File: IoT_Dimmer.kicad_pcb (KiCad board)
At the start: 2 copper layers, 1 part

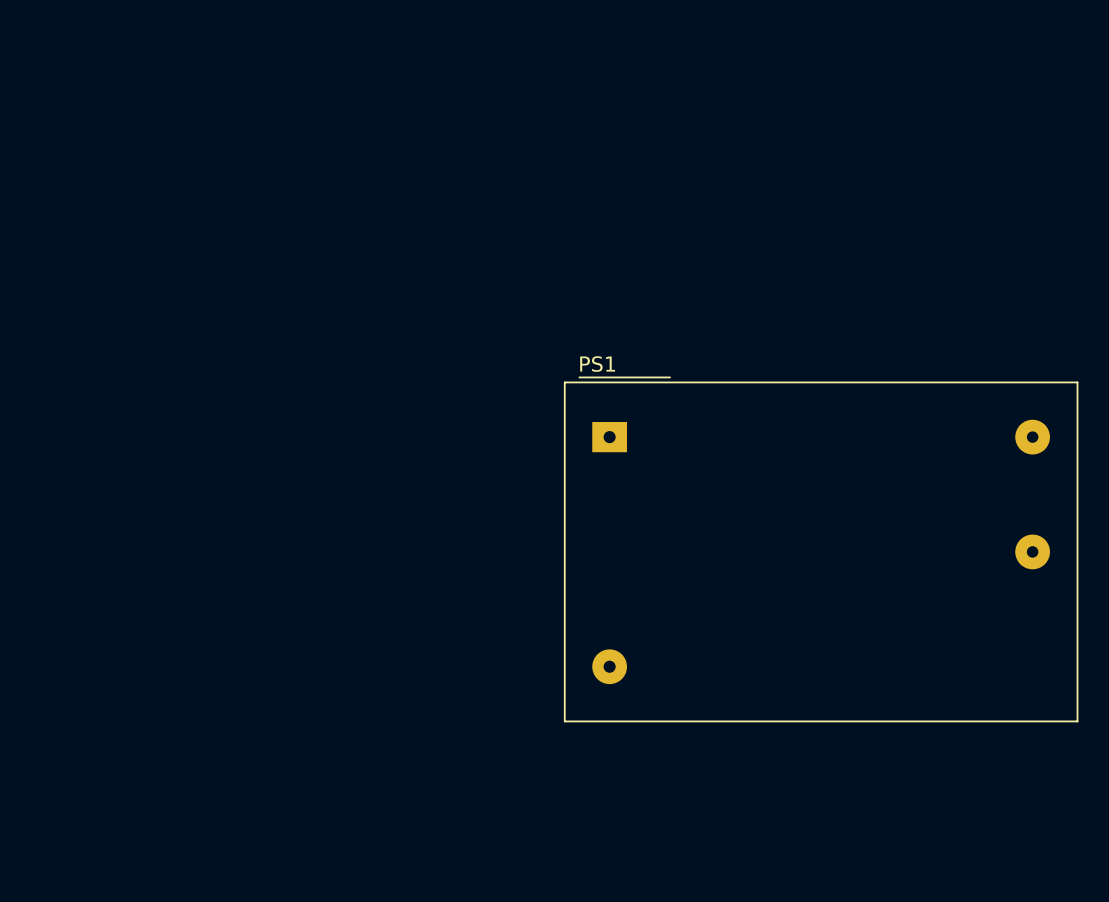
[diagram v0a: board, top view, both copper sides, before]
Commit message: Power esp32
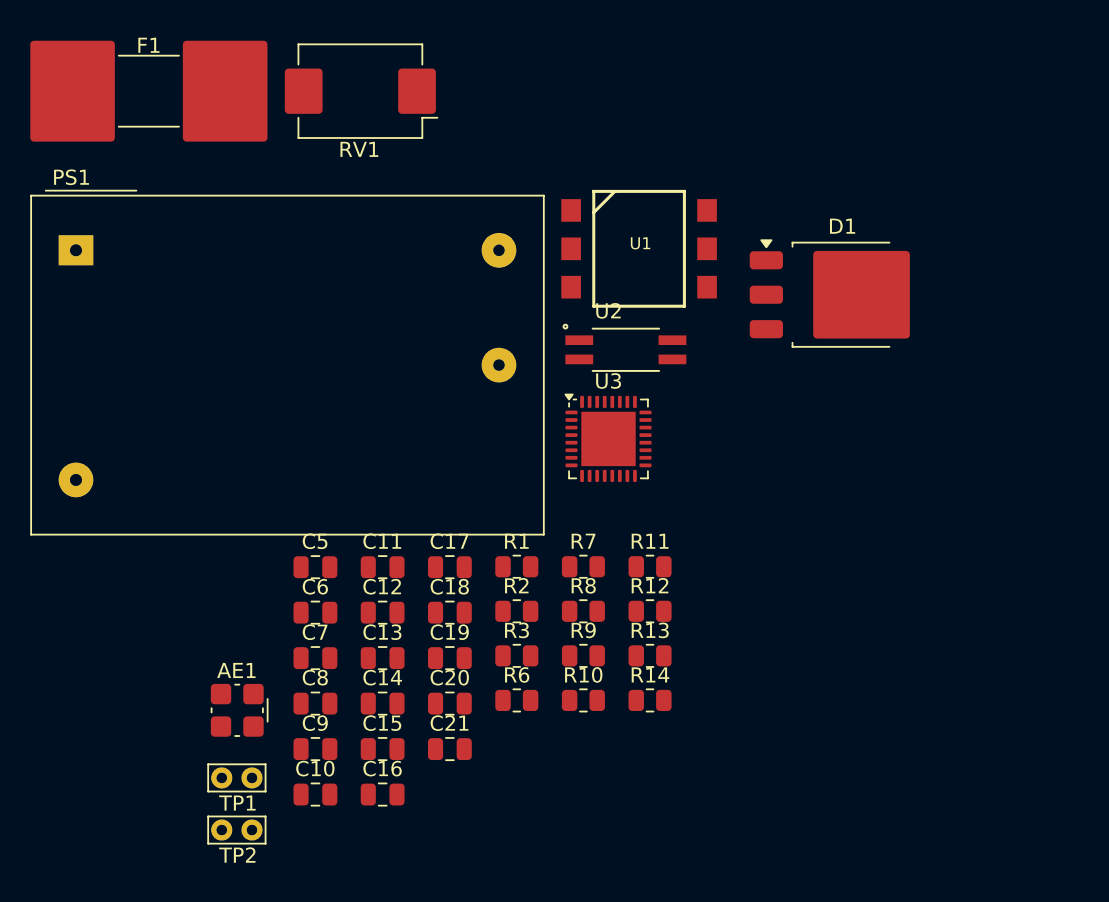
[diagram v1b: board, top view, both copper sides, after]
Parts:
- added AE1: Antenna, RF_Antenna:Molex_47948-0001_2.4Ghz, F.Cu at (119.8, 90.5)
- added C10: 0.1uF, Capacitor_SMD:C_0805_2012Metric, F.Cu at (125.0, 96.1)
- added C11: 0.1uF, Capacitor_SMD:C_0805_2012Metric, F.Cu at (129.5, 81.0)
- added C12: 0.1uF, Capacitor_SMD:C_0805_2012Metric, F.Cu at (129.5, 84.0)
- added C13: 1uF, Capacitor_SMD:C_0805_2012Metric, F.Cu at (129.5, 87.0)
- added C14: 0.1uF, Capacitor_SMD:C_0805_2012Metric, F.Cu at (129.5, 90.0)
- added C15: 0.1uF, Capacitor_SMD:C_0805_2012Metric, F.Cu at (129.5, 93.0)
- added C16: 10nF, Capacitor_SMD:C_0805_2012Metric, F.Cu at (129.5, 96.1)
- added C17: 1uF, Capacitor_SMD:C_0805_2012Metric, F.Cu at (133.9, 81.0)
- added C18: 0.1uF, Capacitor_SMD:C_0805_2012Metric, F.Cu at (133.9, 84.0)
- added C19: 0.1uF, Capacitor_SMD:C_0805_2012Metric, F.Cu at (133.9, 87.0)
- added C20: 0.1uF, Capacitor_SMD:C_0805_2012Metric, F.Cu at (133.9, 90.0)
- added C21: 0.1uF, Capacitor_SMD:C_0805_2012Metric, F.Cu at (133.9, 93.0)
- added C5: 10pF, Capacitor_SMD:C_0805_2012Metric, F.Cu at (125.0, 81.0)
- added C6: 10pF, Capacitor_SMD:C_0805_2012Metric, F.Cu at (125.0, 84.0)
- added C7: 0.1uF, Capacitor_SMD:C_0805_2012Metric, F.Cu at (125.0, 87.0)
- added C8: 0.1uF, Capacitor_SMD:C_0805_2012Metric, F.Cu at (125.0, 90.0)
- added C9: 4.7uF, Capacitor_SMD:C_0805_2012Metric, F.Cu at (125.0, 93.0)
- added D1: BTA204S-800, Package_TO_SOT_SMD:TO-252-3_TabPin2, F.Cu at (159.9, 63.0)
- added F1: 2A, Fuse:Fuse_Littelfuse-NANO2-462, F.Cu at (114.0, 49.5)
- added R1: 360, Resistor_SMD:R_0805_2012Metric, F.Cu at (138.4, 81.0)
- added R10: 510, Resistor_SMD:R_0805_2012Metric, F.Cu at (142.8, 89.8)
- added R11: 10k, Resistor_SMD:R_0805_2012Metric, F.Cu at (147.2, 81.0)
- added R12: 10k, Resistor_SMD:R_0805_2012Metric, F.Cu at (147.2, 83.9)
- added R13: 10k, Resistor_SMD:R_0805_2012Metric, F.Cu at (147.2, 86.9)
- added R14: 10k, Resistor_SMD:R_0805_2012Metric, F.Cu at (147.2, 89.8)
- added R2: 470, Resistor_SMD:R_0805_2012Metric, F.Cu at (138.4, 83.9)
- added R3: 39, Resistor_SMD:R_0805_2012Metric, F.Cu at (138.4, 86.9)
- added R6: 10k, Resistor_SMD:R_0805_2012Metric, F.Cu at (138.4, 89.8)
- added R7: 10k, Resistor_SMD:R_0805_2012Metric, F.Cu at (142.8, 81.0)
- added R8: 10k, Resistor_SMD:R_0805_2012Metric, F.Cu at (142.8, 83.9)
- added R9: 500, Resistor_SMD:R_0805_2012Metric, F.Cu at (142.8, 86.9)
- added RV1: Varistor, Varistor:Varistor_Panasonic_VF, F.Cu at (128.0, 49.5)
- added TP1: RST, TestPoint:TestPoint_Bridge_Pitch2.0mm_Drill0.7mm, F.Cu at (118.8, 95.0)
- added TP2: BOOT, TestPoint:TestPoint_Bridge_Pitch2.0mm_Drill0.7mm, F.Cu at (118.8, 98.4)
- added U1: MOC3021S, MOC3021SM:DIP6_SMD, F.Cu at (146.4, 59.9)
- added U2: VOS628AT, VOS628AT:SOIC127P700X210-4N, F.Cu at (145.6, 66.6)
- added U3: ESP32-C6FH4, Package_DFN_QFN:QFN-32-1EP_5x5mm_P0.5mm_EP3.6x3.6mm, F.Cu at (144.4, 72.5)
- moved PS1 37.4 mm to (109.2, 60.0)
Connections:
- PS1 pad 1: unconnected-(PS1-AC/N-Pad1) -> Net-(D1-A2)
- PS1 pad 2: unconnected-(PS1-AC/L-Pad2) -> Net-(J1-Pin_1)
- PS1 pad 3: unconnected-(PS1--Vo-Pad3) -> GND
- PS1 pad 4: unconnected-(PS1-+Vo-Pad4) -> +3V3

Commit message: PCB_start
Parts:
- added C1: 0.05uF, Capacitor_SMD:C_1812_4532Metric, F.Cu at (174.2, 34.2)
- added C2: 22nF, Capacitor_SMD:C_1812_4532Metric, F.Cu at (194.7, 52.1)
- added C3: C, Capacitor_SMD:C_0603_1608Metric, F.Cu at (162.6, 85.4)
- added C4: C, Capacitor_SMD:C_0603_1608Metric, F.Cu at (162.6, 88.4)
- added J2: Screw_Terminal_01x02, Wago_2059-302998-403:CONN2_2059-302&slash_998-403_WAG, F.Cu at (181.5, 12.5)
- added L1: L, Inductor_SMD:L_0805_2012Metric, F.Cu at (167.1, 85.3)
- added L2: 0.1nH, Inductor_SMD:L_0805_2012Metric, F.Cu at (167.1, 88.0)
- added R4: 75k, Resistor_SMD:R_1206_3216Metric, F.Cu at (168.5, 51.8)
- added R5: 75k, Resistor_SMD:R_1206_3216Metric, F.Cu at (168.5, 48.0)
- added Y2: Crystal_GND24, Crystal:Crystal_SMD_2016-4Pin_2.0x1.6mm, F.Cu at (161.2, 97.0)
- C10, C11, C12, C13, C14, C15, C16, C17, C18, C19, C20, C21, C5, C6, C7, C8, C9: footprint Capacitor_SMD:C_0805_2012Metric -> Capacitor_SMD:C_0603_1608Metric
- F1: value 2A -> 3A
- R1, R2, R3: footprint Resistor_SMD:R_0805_2012Metric -> Resistor_SMD:R_1206_3216Metric
- R10, R11, R12, R13, R14, R6, R7, R8, R9: footprint Resistor_SMD:R_0805_2012Metric -> Resistor_SMD:R_0603_1608Metric
- RV1: footprint Varistor:Varistor_Panasonic_VF -> Varistor:RV_Disc_D7mm_W3.4mm_P5mm
- moved RV1 62.1 mm to (184.0, 22.6)
- moved R2 58.0 mm to (175.0, 39.0)
- moved R1 50.6 mm to (171.8, 43.0)
- moved C5 41.8 mm to (163.7, 97.0), turned to -90 degrees
- moved U3 39.1 mm to (162.8, 107.0)
- moved C17 36.4 mm to (163.4, 102.4)
- moved R3 36.4 mm to (171.5, 72.0)
- moved C6 36.1 mm to (158.8, 97.0), turned to 90 degrees
- moved D1 34.8 mm to (185.2, 39.0)
- moved R9 33.7 mm to (170.0, 106.8)
- moved C16 30.8 mm to (159.5, 103.1), turned to 180 degrees
- moved F1 30.0 mm to (108.5, 20.0)
- moved U1 28.1 mm to (162.2, 36.7)
- moved U2 22.9 mm to (160.8, 49.5), turned to 180 degrees
- moved C15 20.8 mm to (147.5, 103.5)
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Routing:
- net /xtal_p: track 0.00 -> 1.86 mm
- net /xtal_n: track 0.00 -> 1.82 mm

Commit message: CPU_STAND
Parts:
- C2: renamed from C4; footprint Capacitor_SMD:C_0603_1608Metric -> Capacitor_SMD:C_0402_1005Metric
- C4: renamed from C3; footprint Capacitor_SMD:C_0603_1608Metric -> Capacitor_SMD:C_0402_1005Metric
- L1: footprint Inductor_SMD:L_0805_2012Metric -> Inductor_SMD:L_0402_1005Metric
- L2: footprint Inductor_SMD:L_0805_2012Metric -> Inductor_SMD:L_0603_1608Metric
- moved C8 81.6 mm to (167.4, 156.2), turned to 180 degrees
- moved R2 81.1 mm to (173.7, 155.9), turned to -90 degrees
- moved C6 80.8 mm to (171.9, 155.9), turned to -90 degrees
- moved C10 80.4 mm to (166.3, 152.5), turned to -90 degrees
- moved C7 77.6 mm to (167.4, 154.8), turned to 180 degrees
- moved R3 77.0 mm to (170.1, 155.9), turned to -90 degrees
- moved C1 76.4 mm to (164.5, 152.5), turned to -90 degrees
- moved C11 72.0 mm to (175.7, 145.2), turned to 90 degrees
- moved AE1 69.7 mm to (165.1, 143.4), turned to 180 degrees
- moved R1 67.3 mm to (162.8, 152.5), turned to -90 degrees
- moved L2 64.5 mm to (168.1, 152.5), turned to 90 degrees
- moved C4 63.8 mm to (165.7, 149.1), turned to 180 degrees
- moved L1 62.4 mm to (166.2, 147.6), turned to -90 degrees
- moved C2 57.8 mm to (165.7, 146.2), turned to 180 degrees
- moved C9 57.8 mm to (167.4, 157.8), turned to 180 degrees
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- renumbered C7 to C1, C11 to C10, C14 to C11, C16 to C12, C17 to C13, C10 to C14, C9 to C15, C21 to C16, C19 to C17, C1 to C19, C2 to C21, C5 to C3, C6 to C5, C8 to C6, C13 to C7, C12 to C8, C15 to C9, R6 to R1, R4 to R10, R5 to R11, R1 to R12, R2 to R13, R3 to R14, R7 to R2, R8 to R3, R9 to R4, R11 to R5, R10 to R6, R12 to R7, R13 to R8, R14 to R9, TP2 to TP1, TP1 to TP2, U3 to U1, U1 to U3, Y2 to Y1
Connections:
- net /xtal_n renamed /XTAL_N
- net /xtal_p renamed /XTAL_P
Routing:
- net Net-(U1-ANT): track 0.00 -> 3.44 mm
- net Net-(AE1-A): track 0.00 -> 2.64 mm
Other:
- copper layers 2 -> 4

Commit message: pcb
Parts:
- removed TP1: BOOT, TestPoint:TestPoint_Bridge_Pitch2.0mm_Drill0.7mm
- removed TP2: RST, TestPoint:TestPoint_Bridge_Pitch2.0mm_Drill0.7mm
- PS1: moved to B.Cu
- moved C3 74.9 mm to (99.8, 153.9), turned to 0 degrees
- moved PS1 74.4 mm to (128.0, 144.1), turned to 180 degrees
- moved C11 74.2 mm to (101.7, 150.9)
- moved Y1 73.1 mm to (99.7, 156.2), turned to 90 degrees
- moved R4 72.3 mm to (106.9, 149.1), turned to 90 degrees
- moved C13 71.8 mm to (103.2, 150.9), turned to 90 degrees
- moved C5 68.9 mm to (101.7, 156.2)
- moved AE1 68.1 mm to (99.2, 160.8), turned to -90 degrees
- moved C12 66.4 mm to (103.2, 157.0), turned to -90 degrees
- moved C2 65.3 mm to (102.0, 160.2), turned to -90 degrees
- moved U1 65.0 mm to (107.1, 153.9), turned to 90 degrees
- moved L1 63.9 mm to (103.4, 159.7), turned to 0 degrees
- moved R2 62.1 mm to (111.7, 152.2), turned to 0 degrees
- moved C4 61.9 mm to (104.9, 160.2), turned to -90 degrees
- moved L2 60.4 mm to (108.3, 160.7), turned to 180 degrees
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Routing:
- net /chip_pu/rst: track 0.00 -> 3.17 mm
- net /XTAL_N: track 1.91 -> 0.00 mm
- net +3V3: track 0.00 -> 1.63 mm
- net /XTAL_P: track 1.58 -> 0.00 mm
- net GND: vias 0 -> 16
